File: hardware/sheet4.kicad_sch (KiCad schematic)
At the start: 27 parts, among them J2 B4B-XH-A, J3 B-2100S04P-A110, J4 U254-051N-4BH806, U2 STM32F072CBT6, U4 USBLC6-2SC6, Y1 32.768kHz

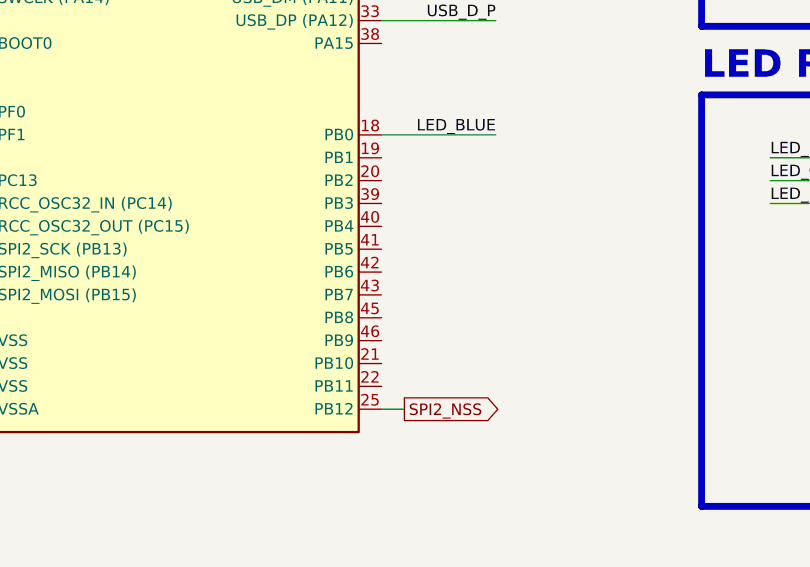
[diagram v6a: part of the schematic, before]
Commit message: hardware(feat): add lm75bd temperature sensor on i2c1 (#4)
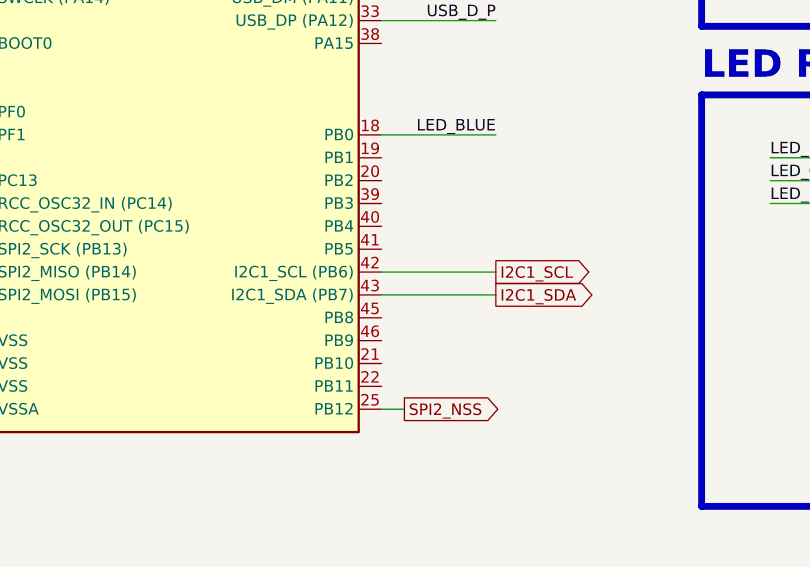
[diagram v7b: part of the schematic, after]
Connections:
- net I2C1_SCL: now reaches U2.42 (PB6)
- net I2C1_SDA: now reaches U2.43 (PB7)
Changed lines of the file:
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@@
 	(wire
 		(pts
+			(xy 185.42 132.08) (xy 198.12 132.08)
+		)
+		(stroke
+			(width 0)
+			(type default)
+		)
+	)
+	(wire
+		(pts
 			(xy 185.42 116.84) (xy 198.12 116.84)
 		)
@@
 	(wire
 		(pts
+			(xy 185.42 134.62) (xy 198.12 134.62)
+		)
+		(stroke
+			(width 0)
+			(type default)
+		)
+	)
+	(wire
+		(pts
 			(xy 96.52 73.66) (xy 106.68 73.66)
 		)
@@
 		)
 	)
+	(global_label "I2C1_SCL"
+		(shape output)
+		(at 198.12 132.08 0)
+		(fields_autoplaced yes)
+		(effects
+			(font
+				(size 1.27 1.27)
+			)
+			(justify left)
+		)
+		(property "Intersheetrefs" "${INTERSHEET_REFS}"
+			(at 209.8742 132.08 0)
+			(effects
+				(font
+					(size 1.27 1.27)
+				)
+				(justify left)
+				(hide yes)
+			)
+		)
+	)
 	(global_label "SPI2_NSS"
 		(shape output)
@@
 		)
 	)
+	(global_label "I2C1_SDA"
+		(shape output)
+		(at 198.12 134.62 0)
+		(fields_autoplaced yes)
+		(effects
+			(font
+				(size 1.27 1.27)
+			)
+			(justify left)
+		)
+		(property "Intersheetrefs" "${INTERSHEET_REFS}"
+			(at 209.9347 134.62 0)
+			(effects
+				(font
+					(size 1.27 1.27)
+				)
+				(justify left)
+				(hide yes)
+			)
+		)
+	)
 	(symbol
 		(lib_id "power:GND")
@@
 		)
 		(pin "42"
+			(alternate "I2C1_SCL (PB6)")
 		)
 		(pin "40"
@@
 		)
 		(pin "43"
+			(alternate "I2C1_SDA (PB7)")
 		)
 		(pin "34"

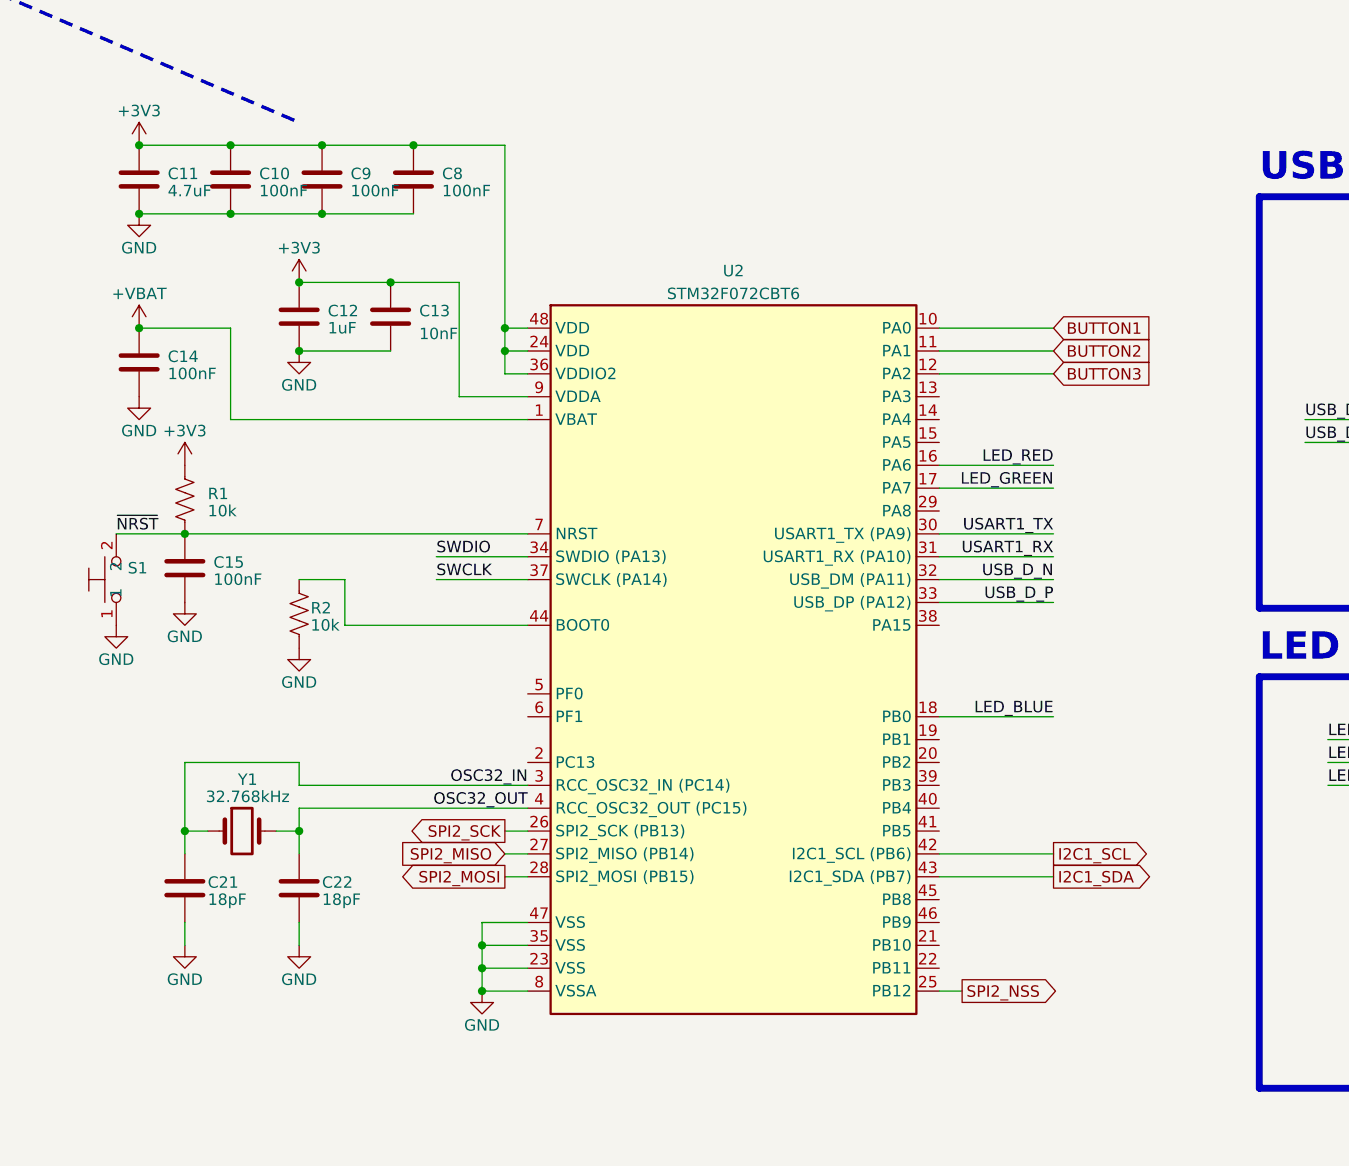
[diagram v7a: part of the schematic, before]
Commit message: hardware(feat): add esp-01 wifi module on usart3
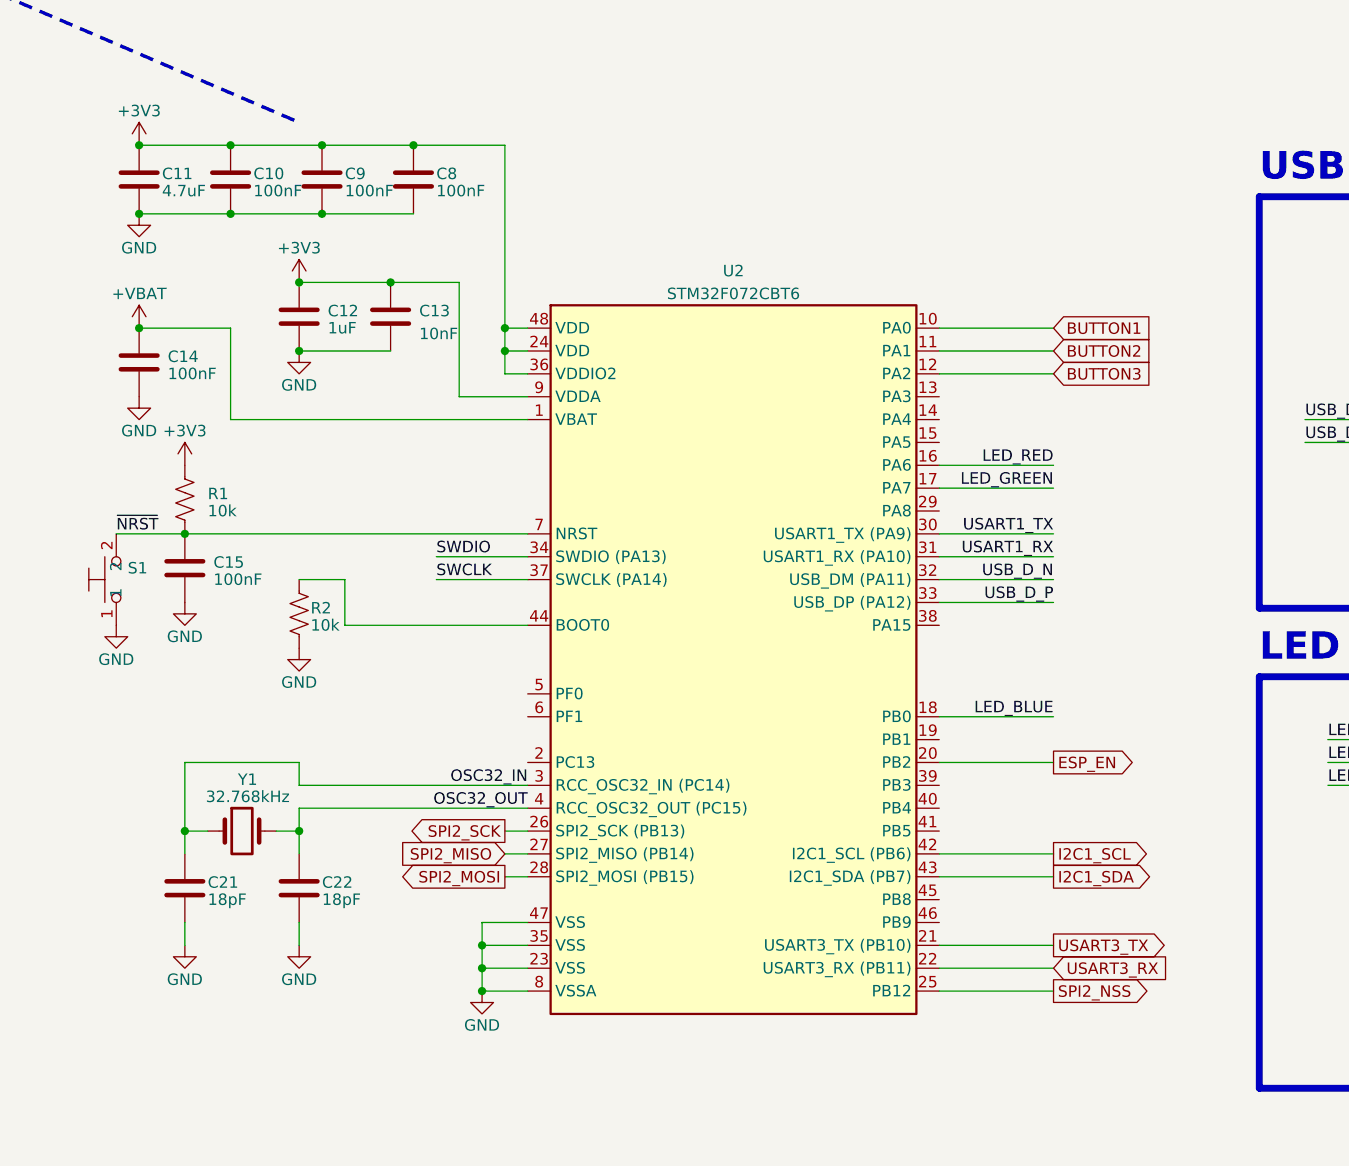
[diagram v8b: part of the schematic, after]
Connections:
- net ESP_EN: now reaches U2.20 (PB2)
- net USART3_TX: now reaches U2.21 (PB10)
- net USART3_RX: now reaches U2.22 (PB11)
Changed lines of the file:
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@@
 	(wire
 		(pts
-			(xy 185.42 147.32) (xy 187.96 147.32)
+			(xy 185.42 147.32) (xy 198.12 147.32)
 		)
 		(stroke
@@
 	(wire
 		(pts
+			(xy 185.42 142.24) (xy 198.12 142.24)
+		)
+		(stroke
+			(width 0)
+			(type default)
+		)
+	)
+	(wire
+		(pts
 			(xy 134.62 144.78) (xy 139.7 144.78)
 		)
@@
 	(wire
 		(pts
+			(xy 185.42 144.78) (xy 198.12 144.78)
+		)
+		(stroke
+			(width 0)
+			(type default)
+		)
+	)
+	(wire
+		(pts
 			(xy 129.54 99.06) (xy 139.7 99.06)
 		)
@@
 	(wire
 		(pts
+			(xy 185.42 121.92) (xy 198.12 121.92)
+		)
+		(stroke
+			(width 0)
+			(type default)
+		)
+	)
+	(wire
+		(pts
 			(xy 93.98 96.52) (xy 101.6 96.52)
 		)
@@
 	(global_label "SPI2_NSS"
 		(shape output)
-		(at 187.96 147.32 0)
+		(at 198.12 147.32 0)
 		(fields_autoplaced yes)
 		(effects
@@
 		)
 		(property "Intersheetrefs" "${INTERSHEET_REFS}"
-			(at 199.9561 147.32 0)
+			(at 210.1161 147.32 0)
 			(effects
 				(font
@@
 		)
 	)
+	(global_label "USART3_RX"
+		(shape input)
+		(at 198.12 144.78 0)
+		(fields_autoplaced yes)
+		(effects
+			(font
+				(size 1.27 1.27)
+			)
+			(justify left)
+		)
+		(property "Intersheetrefs" "${INTERSHEET_REFS}"
+			(at 211.628 144.78 0)
+			(effects
+				(font
+					(size 1.27 1.27)
+				)
+				(justify left)
+				(hide yes)
+			)
+		)
+	)
 	(global_label "BUTTON3"
 		(shape input)
@@
 		)
 	)
+	(global_label "ESP_EN"
+		(shape output)
+		(at 198.12 121.92 0)
+		(fields_autoplaced yes)
+		(effects
+			(font
+				(size 1.27 1.27)
+			)
+			(justify left)
+		)
+		(property "Intersheetrefs" "${INTERSHEET_REFS}"
+			(at 208.1808 121.92 0)
+			(effects
+				(font
+					(size 1.27 1.27)
+				)
+				(justify left)
+				(hide yes)
+			)
+		)
+	)
 	(global_label "BUTTON2"
 		(shape input)
@@
 		)
 	)
+	(global_label "USART3_TX"
+		(shape output)
+		(at 198.12 142.24 0)
+		(fields_autoplaced yes)
+		(effects
+			(font
+				(size 1.27 1.27)
+			)
+			(justify left)
+		)
+		(property "Intersheetrefs" "${INTERSHEET_REFS}"
+			(at 211.3256 142.24 0)
+			(effects
+				(font
+					(size 1.27 1.27)
+				)
+				(justify left)
+				(hide yes)
+			)
+		)
+	)
 	(global_label "I2C1_SDA"
 		(shape output)
@@
 		(dnp no)
 		(property "Reference" "C10"
-			(at 109.855 56.515 0)
+			(at 109.22 56.515 0)
 			(effects
 				(font
@@
 		)
 		(property "Value" "100nF"
-			(at 109.855 58.42 0)
+			(at 109.22 58.42 0)
 			(effects
 				(font
@@
 		(dnp no)
 		(property "Reference" "C9"
-			(at 120.015 56.515 0)
+			(at 119.38 56.515 0)
 			(effects
 				(font
@@
 		)
 		(property "Value" "100nF"
-			(at 120.015 58.42 0)
+			(at 119.38 58.42 0)
 			(effects
 				(font
@@
 		(dnp no)
 		(property "Reference" "C11"
-			(at 99.695 56.515 0)
+			(at 99.06 56.515 0)
 			(effects
 				(font
@@
 		)
 		(property "Value" "4.7uF"
-			(at 99.695 58.42 0)
+			(at 99.06 58.42 0)
 			(effects
 				(font
@@
 		)
 		(pin "22"
+			(alternate "USART3_RX (PB11)")
 		)
 		(pin "45"
 		)
 		(pin "21"
+			(alternate "USART3_TX (PB10)")
 		)
 		(pin "25"
@@
 		(dnp no)
 		(property "Reference" "C8"
-			(at 130.175 56.515 0)
+			(at 129.54 56.515 0)
 			(effects
 				(font
@@
 		)
 		(property "Value" "100nF"
-			(at 130.175 58.42 0)
+			(at 129.54 58.42 0)
 			(effects
 				(font
